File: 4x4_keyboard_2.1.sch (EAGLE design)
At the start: 74 parts, among them U2 AMS1117-5.0

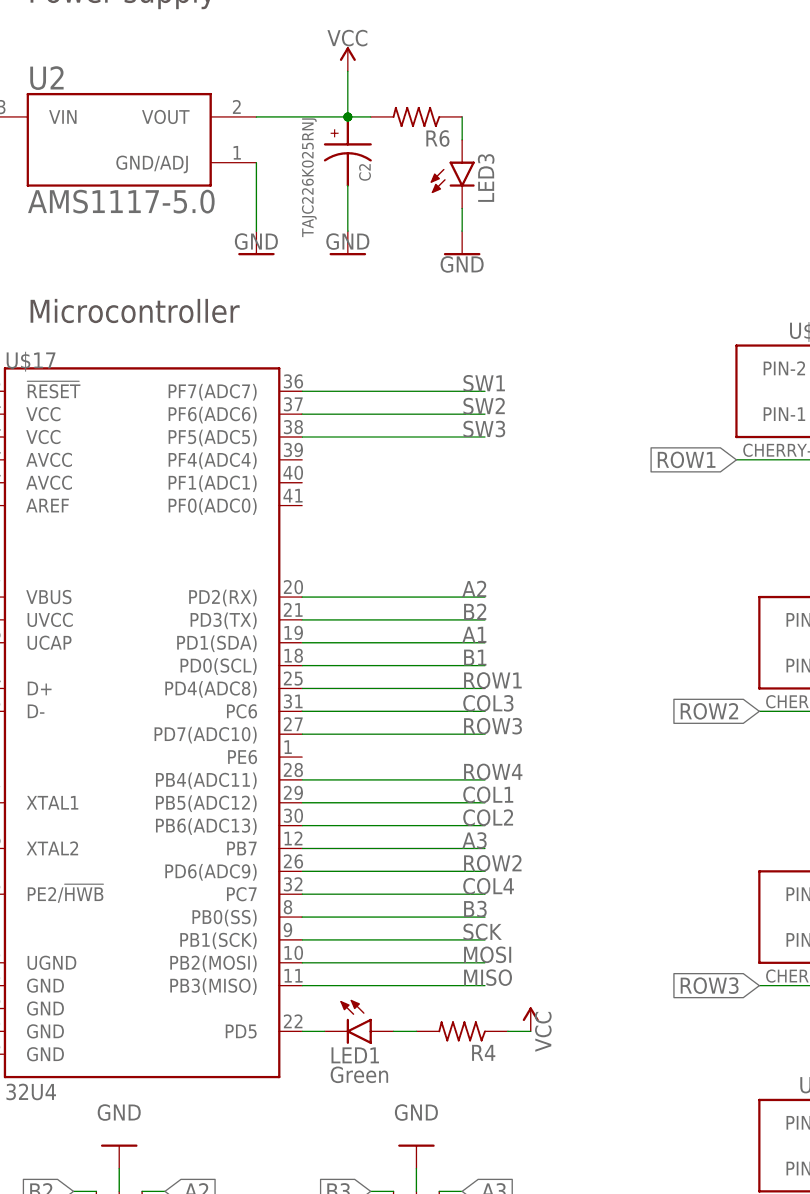
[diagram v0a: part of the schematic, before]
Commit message: switch routing
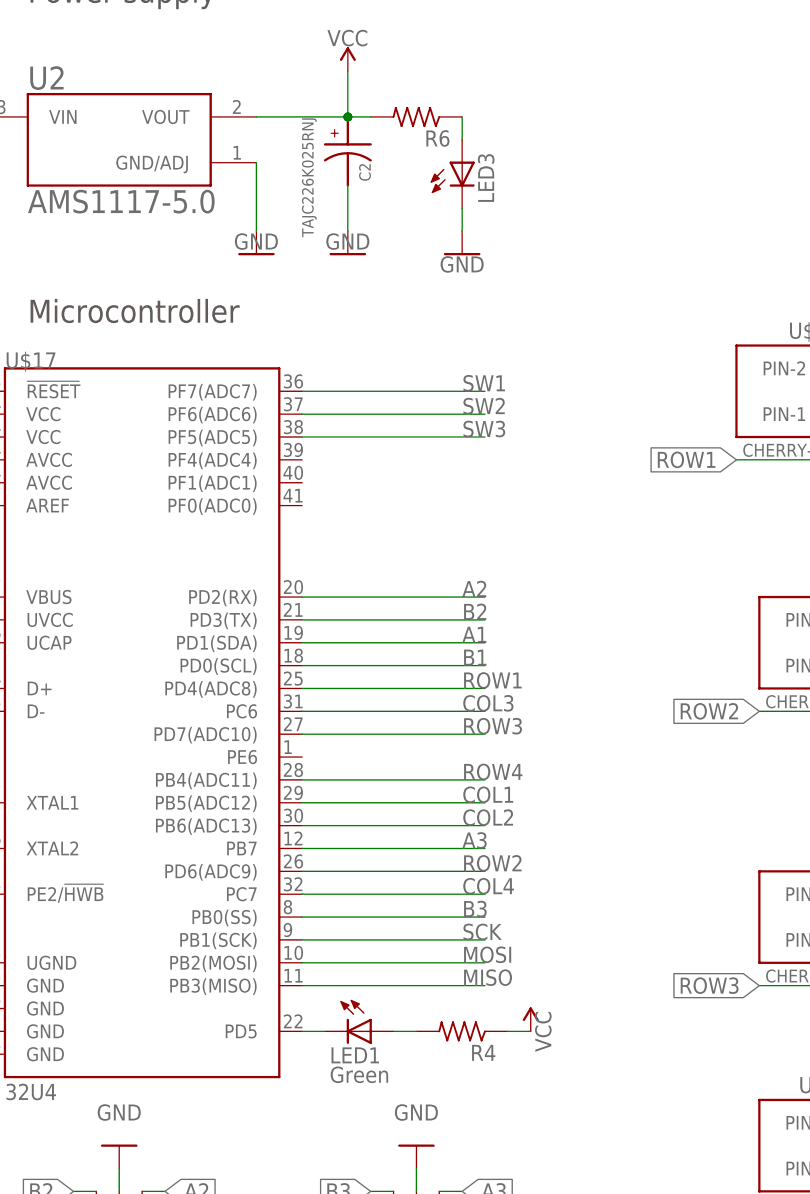
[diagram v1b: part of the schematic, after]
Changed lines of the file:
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@@
 <?xml version="1.0" encoding="utf-8"?>
 <!DOCTYPE eagle SYSTEM "eagle.dtd">
-<eagle version="9.6.2">
+<eagle version="6.4">
 <drawing>
 <settings>
 <setting alwaysvectorfont="no"/>
-<setting keepoldvectorfont="yes"/>
 <setting verticaltext="up"/>
 </settings>
@@
 <part name="SJ15" library="jumper" deviceset="SJ" device=""/>
 <part name="SJ16" library="jumper" deviceset="SJ" device=""/>
-<part name="C10" library="rcl" library_urn="urn:adsk.eagle:library:334" deviceset="C-EU" device="C0603" package3d_urn="urn:adsk.eagle:package:23616/2" value="1.0uF"/>
-<part name="C3" library="rcl" library_urn="urn:adsk.eagle:library:334" deviceset="C-EU" device="C0603" package3d_urn="urn:adsk.eagle:package:23616/2" value="0.1uF"/>
-<part name="C1" library="rcl" library_urn="urn:adsk.eagle:library:334" deviceset="C-EU" device="C0603" package3d_urn="urn:adsk.eagle:package:23616/2" value="0.1uF"/>
-<part name="C5" library="rcl" library_urn="urn:adsk.eagle:library:334" deviceset="C-EU" device="C0603" package3d_urn="urn:adsk.eagle:package:23616/2" value="1.0uF"/>
-<part name="C6" library="rcl" library_urn="urn:adsk.eagle:library:334" deviceset="C-EU" device="C0603" package3d_urn="urn:adsk.eagle:package:23616/2" value="1.0uF"/>
+<part name="C10" library="rcl" deviceset="C-EU" device="C0603" value="1.0uF"/>
+<part name="C3" library="rcl" deviceset="C-EU" device="C0603" value="0.1uF"/>
+<part name="C1" library="rcl" deviceset="C-EU" device="C0603" value="0.1uF"/>
+<part name="C5" library="rcl" deviceset="C-EU" device="C0603" value="1.0uF"/>
+<part name="C6" library="rcl" deviceset="C-EU" device="C0603" value="1.0uF"/>
 <part name="GND4" library="SparkFun-PowerSymbols" deviceset="GND" device=""/>
 <part name="GND8" library="SparkFun-PowerSymbols" deviceset="GND" device=""/>
@@
 <part name="SUPPLY5" library="SparkFun-PowerSymbols" deviceset="V_USB" device=""/>
 <part name="GND5" library="SparkFun-PowerSymbols" deviceset="GND" device=""/>
-<part name="C7" library="rcl" library_urn="urn:adsk.eagle:library:334" deviceset="C-EU" device="C0603" package3d_urn="urn:adsk.eagle:package:23616/2" value="10uF"/>
+<part name="C7" library="rcl" deviceset="C-EU" device="C0603" value="10uF"/>
 <part name="GND18" library="SparkFun-PowerSymbols" deviceset="GND" device=""/>
 <part name="SUPPLY9" library="SparkFun-PowerSymbols" deviceset="VCC" device=""/>
 <part name="LED3" library="led" deviceset="LED" device="SML0805"/>
-<part name="R6" library="audio amplifier example" library_urn="urn:adsk.eagle:library:970892" deviceset="R-US_" device="R0603" package3d_urn="urn:adsk.eagle:package:970938/2" value="1K"/>
+<part name="R6" library="audio amplifier example" deviceset="R-US_" device="R0603" value="1K"/>
 <part name="GND22" library="SparkFun-PowerSymbols" deviceset="GND" device=""/>
 <part name="SUPPLY10" library="SparkFun-PowerSymbols" deviceset="V_USB" device=""/>
@@
 <part name="U$17" library="SparkFun-IC-Microcontroller" deviceset="ATMEGA32U4" device="TQFP-44" value="32U4"/>
 <part name="LED1" library="led" deviceset="LED" device="SML0805" value="Green"/>
-<part name="R4" library="audio amplifier example" library_urn="urn:adsk.eagle:library:970892" deviceset="R-US_" device="R0603" package3d_urn="urn:adsk.eagle:package:970938/2" value="1K"/>
+<part name="R4" library="audio amplifier example" deviceset="R-US_" device="R0603" value="1K"/>
 <part name="SUPPLY1" library="SparkFun-PowerSymbols" deviceset="VCC" device=""/>
 <part name="SUPPLY4" library="SparkFun-PowerSymbols" deviceset="V_USB" device=""/>
 <part name="SUPPLY11" library="SparkFun-PowerSymbols" deviceset="VCC" device=""/>
-<part name="R7" library="audio amplifier example" library_urn="urn:adsk.eagle:library:970892" deviceset="R-US_" device="R0603" package3d_urn="urn:adsk.eagle:package:970938/2" value="1K"/>
+<part name="R7" library="audio amplifier example" deviceset="R-US_" device="R0603" value="1K"/>
 <part name="SUPPLY12" library="SparkFun-PowerSymbols" deviceset="VCC" device=""/>
 <part name="S2" library="SparkFun-Switches" deviceset="MOMENTARY-SWITCH-SPST" device="-SMD-4.6X2.8MM" value="Reset"/>
 <part name="GND13" library="SparkFun-PowerSymbols" deviceset="GND" device=""/>
-<part name="C12" library="rcl" library_urn="urn:adsk.eagle:library:334" deviceset="C-EU" device="C0603" package3d_urn="urn:adsk.eagle:package:23616/2" value="22pF"/>
-<part name="C13" library="rcl" library_urn="urn:adsk.eagle:library:334" deviceset="C-EU" device="C0603" package3d_urn="urn:adsk.eagle:package:23616/2" value="22pF"/>
+<part name="C12" library="rcl" deviceset="C-EU" device="C0603" value="22pF"/>
+<part name="C13" library="rcl" deviceset="C-EU" device="C0603" value="22pF"/>
 <part name="GND23" library="SparkFun-PowerSymbols" deviceset="GND" device=""/>
 <part name="GND24" library="SparkFun-PowerSymbols" deviceset="GND" device=""/>
-<part name="R1" library="audio amplifier example" library_urn="urn:adsk.eagle:library:970892" deviceset="R-US_" device="R0603" package3d_urn="urn:adsk.eagle:package:970938/2" value="22"/>
-<part name="R2" library="audio amplifier example" library_urn="urn:adsk.eagle:library:970892" deviceset="R-US_" device="R0603" package3d_urn="urn:adsk.eagle:package:970938/2" value="22"/>
+<part name="R1" library="audio amplifier example" deviceset="R-US_" device="R0603" value="22"/>
+<part name="R2" library="audio amplifier example" deviceset="R-US_" device="R0603" value="22"/>
 <part name="Q1" library="crystal" deviceset="CRYSTAL" device="HC49UP"/>
 <part name="U2" library="AMS1117-5.0" deviceset="AMS1117-5.0" device=""/>
@@
 </schematic>
 </drawing>
-<compatibility>
-<note version="8.2" severity="warning">
-Since Version 8.2, EAGLE supports online libraries. The ids
-of those online libraries will not be understood (or retained)
-with this version.
-</note>
-<note version="8.3" severity="warning">
-Since Version 8.3, EAGLE supports URNs for individual library
-assets (packages, symbols, and devices). The URNs of those assets
-will not be understood (or retained) with this version.
-</note>
-<note version="8.3" severity="warning">
-Since Version 8.3, EAGLE supports the association of 3D packages
-with devices in libraries, schematics, and board files. Those 3D
-packages will not be understood (or retained) with this version.
-</note>
-<note version="8.4" severity="warning">
-Since Version 8.4, EAGLE supports properties for SPICE simulation.
-Probes in schematics and SPICE mapping objects found in parts and library devices
-will not be understood with this version. Update EAGLE to the latest version
-for full support of SPICE simulation.
-</note>
-</compatibility>
 </eagle>
